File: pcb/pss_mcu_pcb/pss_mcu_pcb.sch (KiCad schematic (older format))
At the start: 50 parts, among them J1 STM32_Prog, J2 UART_Prog, J3 Conn_01x18, J4 Conn_01x18, SW1 Boot, SW2 EN, SW3 SW_Push, U1 LM3940IMP-3.3_NOPB, U2 LM358, U3 STM32F030K6Tx, U4 ESP32-WROOM-32U

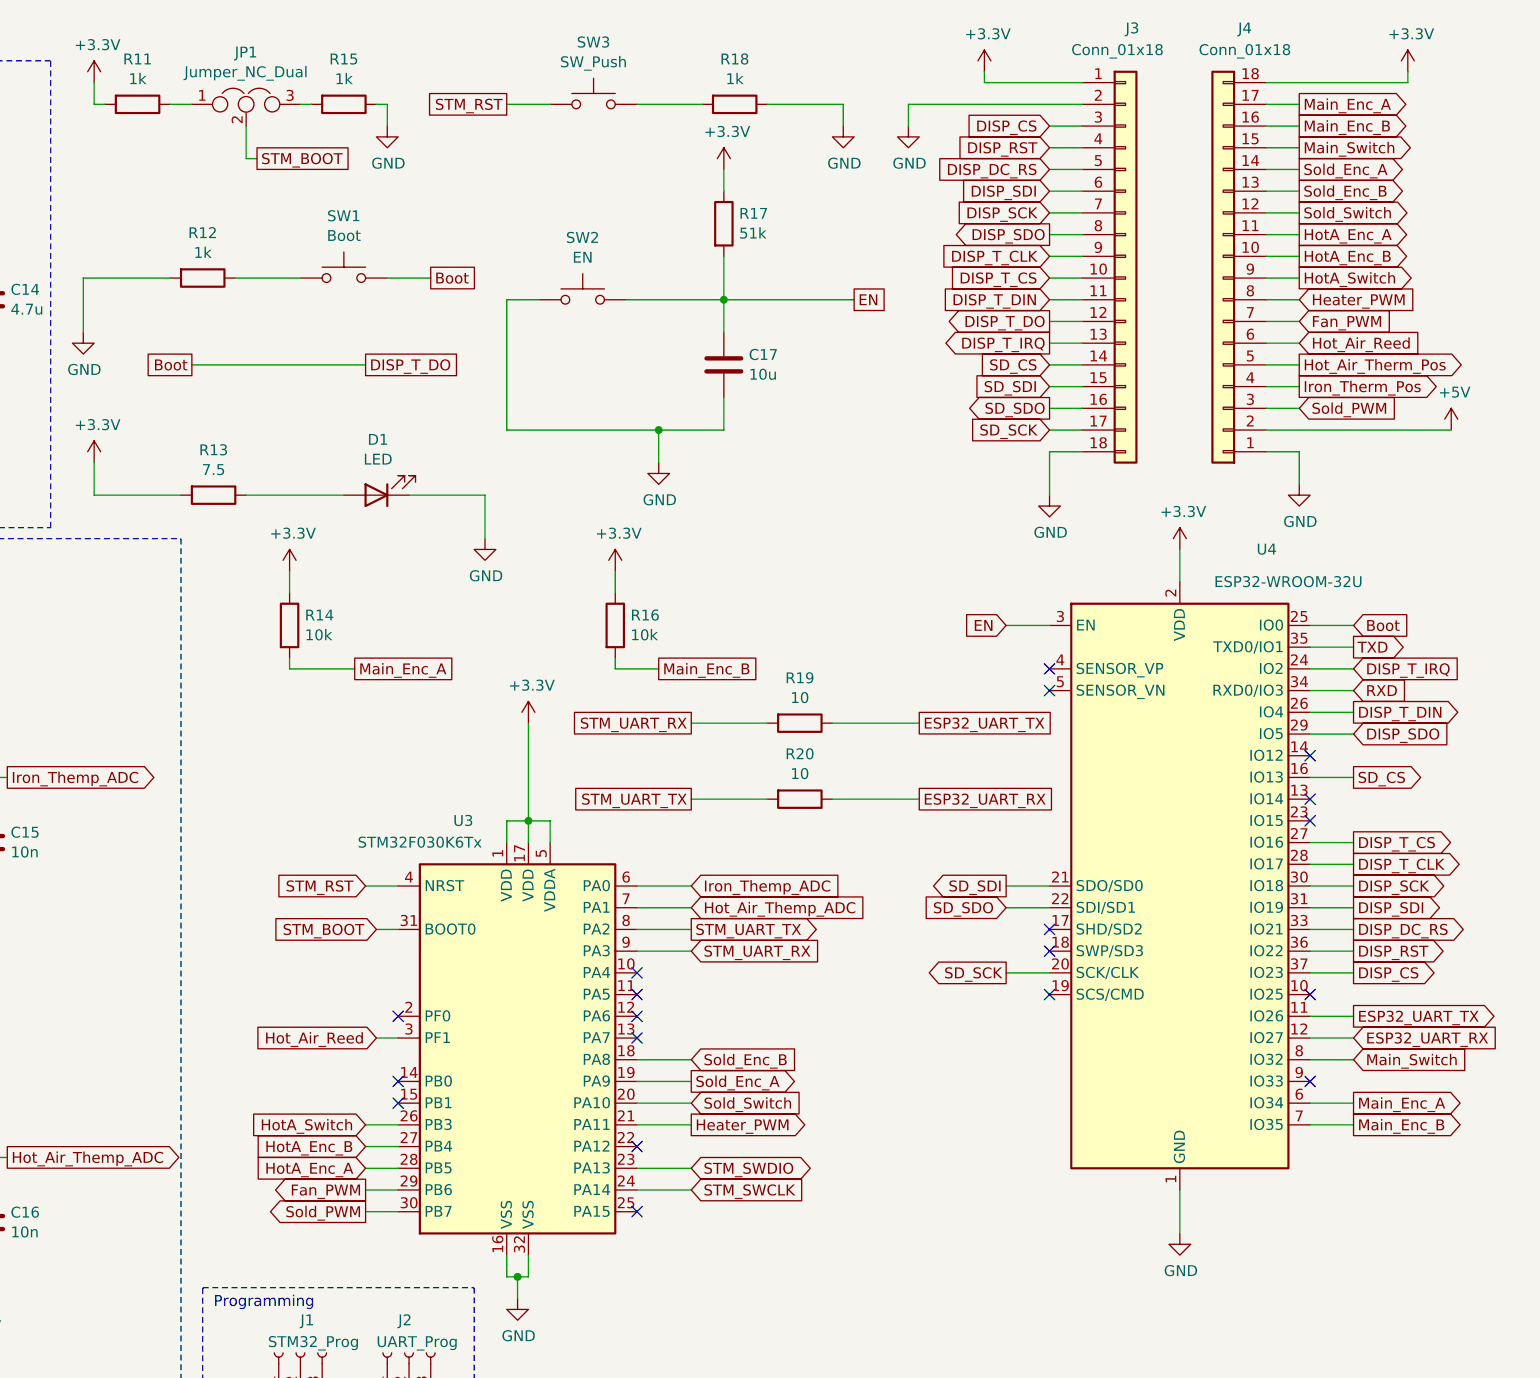
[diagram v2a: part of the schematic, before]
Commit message: Change elements placement
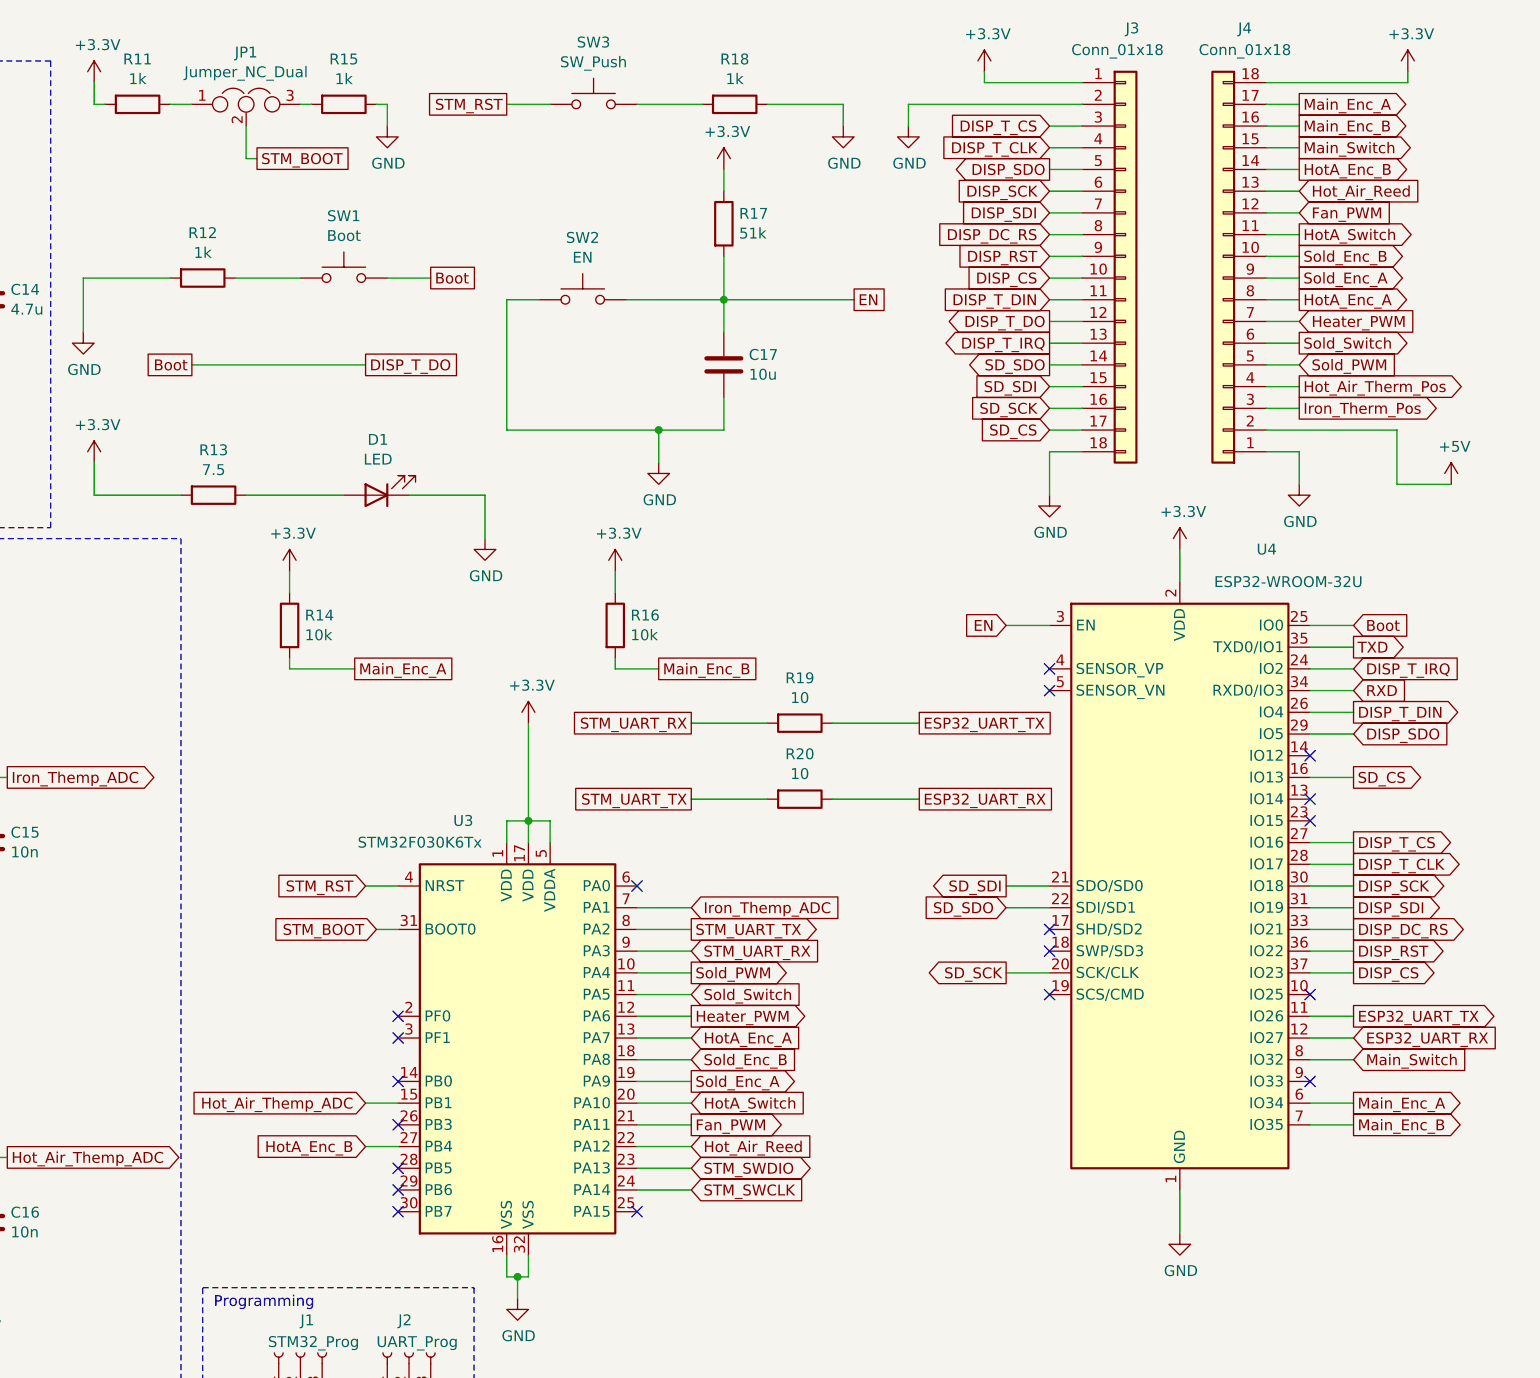
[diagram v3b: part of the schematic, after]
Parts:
- D1: footprint LED_THT:LED_D5.0mm -> LED_SMD:LED_0603_1608Metric_Pad1.05x0.95mm_HandSolder
- SW1, SW2, SW3: footprint Button_Switch_SMD:SW_SPST_B3S-1000 -> Button_Switch_SMD:SW_SPST_B3U-1000P
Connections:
- net DISP_CS: now also J3.10 (Pin_10); no longer J3.3 (Pin_3)
- net DISP_DC_RS: now also J3.8 (Pin_8); no longer J3.5 (Pin_5)
- net DISP_RST: now also J3.9 (Pin_9); no longer J3.4 (Pin_4)
- net DISP_SCK: now also J3.6 (Pin_6); no longer J3.7 (Pin_7)
- net DISP_SDI: now also J3.7 (Pin_7); no longer J3.6 (Pin_6)
- net DISP_SDO: now also J3.5 (Pin_5); no longer J3.8 (Pin_8)
- net DISP_T_CLK: now also J3.4 (Pin_4); no longer J3.9 (Pin_9)
- net DISP_T_CS: now also J3.3 (Pin_3); no longer J3.10 (Pin_10)
- net Fan_PWM: now also J4.12 (Pin_12), U3.21 (PA11); no longer J4.7 (Pin_7), U3.29 (PB6)
- net Heater_PWM: now also J4.7 (Pin_7), U3.12 (PA6); no longer J4.8 (Pin_8), U3.21 (PA11)
- net HotA_Enc_A: now also J4.8 (Pin_8), U3.13 (PA7); no longer J4.11 (Pin_11), U3.28 (PB5)
- net HotA_Enc_B: now also J4.14 (Pin_14); no longer J4.10 (Pin_10)
- net HotA_Switch: now also J4.11 (Pin_11), U3.20 (PA10); no longer J4.9 (Pin_9), U3.26 (PB3)
- net Hot_Air_Reed: now also J4.13 (Pin_13), U3.22 (PA12); no longer J4.6 (Pin_6), U3.3 (PF1)
- net Hot_Air_Themp_ADC: now also U3.15 (PB1); no longer U3.7 (PA1)
- net Hot_Air_Therm_Pos: now also J4.4 (Pin_4); no longer J4.5 (Pin_5)
- net Iron_Themp_ADC: now also U3.7 (PA1); no longer U3.6 (PA0)
- net Iron_Therm_Pos: now also J4.3 (Pin_3); no longer J4.4 (Pin_4)
- net SD_CS: now also J3.17 (Pin_17); no longer J3.14 (Pin_14)
- net SD_SCK: now also J3.16 (Pin_16); no longer J3.17 (Pin_17)
- net SD_SDO: now also J3.14 (Pin_14); no longer J3.16 (Pin_16)
- net Sold_Enc_A: now also J4.9 (Pin_9); no longer J4.14 (Pin_14)
- net Sold_Enc_B: now also J4.10 (Pin_10); no longer J4.13 (Pin_13)
- net Sold_PWM: now also J4.5 (Pin_5), U3.10 (PA4); no longer J4.3 (Pin_3), U3.30 (PB7)
- net Sold_Switch: now also J4.6 (Pin_6), U3.11 (PA5); no longer J4.12 (Pin_12), U3.20 (PA10)
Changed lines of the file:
@@
 F 0 "SW2" H 7100 2085 50  0000 C CNN
 F 1 "EN" H 7100 1994 50  0000 C CNN
-F 2 "Button_Switch_SMD:SW_SPST_B3S-1000" H 7100 2000 50  0001 C CNN
+F 2 "Button_Switch_SMD:SW_SPST_B3U-1000P" H 7100 2000 50  0001 C CNN
 F 3 "~" H 7100 2000 50  0001 C CNN
 	1    7100 1800
@@
 F 0 "SW1" H 6000 1985 50  0000 C CNN
 F 1 "Boot" H 6000 1894 50  0000 C CNN
-F 2 "Button_Switch_SMD:SW_SPST_B3S-1000" H 6000 1900 50  0001 C CNN
+F 2 "Button_Switch_SMD:SW_SPST_B3U-1000P" H 6000 1900 50  0001 C CNN
 F 3 "~" H 6000 1900 50  0001 C CNN
 	1    6000 1700
@@
 F 0 "D1" H 6143 2445 50  0000 C CNN
 F 1 "LED" H 6143 2536 50  0000 C CNN
-F 2 "LED_THT:LED_D5.0mm" H 6150 2700 50  0001 C CNN
+F 2 "LED_SMD:LED_0603_1608Metric_Pad1.05x0.95mm_HandSolder" H 6150 2700 50  0001 C CNN
 F 3 "~" H 6150 2700 50  0001 C CNN
 	1    6150 2700
@@
 F 0 "SW3" H 7150 1185 50  0000 C CNN
 F 1 "SW_Push" H 7150 1094 50  0000 C CNN
-F 2 "Button_Switch_SMD:SW_SPST_B3S-1000" H 7150 1100 50  0001 C CNN
+F 2 "Button_Switch_SMD:SW_SPST_B3U-1000P" H 7150 1100 50  0001 C CNN
 F 3 "~" H 7150 1100 50  0001 C CNN
 	1    7150 900
@@
 $EndComp
 NoConn ~ 6250 5100
-NoConn ~ 7350 5000
-NoConn ~ 7350 5100
-NoConn ~ 7350 5200
-Wire Wire Line
-	6100 5800 6250 5800
 Wire Wire Line
 	6100 5700 6250 5700
 Wire Wire Line
-	6100 5600 6250 5600
-Wire Wire Line
 	7600 5600 7350 5600
-Wire Wire Line
-	6250 5900 6100 5900
-Wire Wire Line
-	6250 5200 6150 5200
-NoConn ~ 7350 5700
-NoConn ~ 6250 5500
-NoConn ~ 6250 5400
-Text GLabel 7600 5600 2    50   Output ~ 0
+Text GLabel 7600 5100 2    50   Output ~ 0
 Heater_PWM
-Wire Wire Line
-	6250 6000 6100 6000
-Text GLabel 6100 6000 0    50   Output ~ 0
+Text GLabel 7600 4900 2    50   Output ~ 0
 Sold_PWM
-Text GLabel 6150 5200 0    50   Input ~ 0
+Text GLabel 7600 5700 2    50   Input ~ 0
 Hot_Air_Reed
 Wire Wire Line
@@
 Text GLabel 7600 5900 2    50   Input ~ 0
 STM_SWCLK
-Text GLabel 6100 5900 0    50   Output ~ 0
+Text GLabel 7600 5600 2    50   Output ~ 0
 Fan_PWM
 Wire Wire Line
 	7350 5500 7600 5500
-Text GLabel 6100 5600 0    50   Input ~ 0
+Text GLabel 7600 5500 2    50   Input ~ 0
 HotA_Switch
 Wire Wire Line
@@
 Wire Wire Line
 	7350 5300 7600 5300
-Text GLabel 6100 5800 0    50   Input ~ 0
+Text GLabel 7600 5200 2    50   Input ~ 0
 HotA_Enc_A
 Text GLabel 7600 5300 2    50   Input ~ 0
@@
 Text GLabel 7600 5400 2    50   Output ~ 0
 Sold_Enc_A
-NoConn ~ 7350 4900
-Text GLabel 7600 5500 2    50   Input ~ 0
+Text GLabel 7600 5000 2    50   Input ~ 0
 Sold_Switch
 Wire Wire Line
@@
 Text GLabel 7600 4700 2    50   Output ~ 0
 STM_UART_TX
-Wire Wire Line
-	7600 4600 7350 4600
-Wire Wire Line
-	7350 4500 7600 4500
+Text GLabel 6100 5500 0    50   Input ~ 0
+Hot_Air_Themp_ADC
 Text GLabel 7600 4600 2    50   Input ~ 0
-Hot_Air_Themp_ADC
-Text GLabel 7600 4500 2    50   Input ~ 0
 Iron_Themp_ADC
 Wire Wire Line
@@
 Wire Wire Line
 	9250 2100 9400 2100
-Text GLabel 10400 2100 2    50   Output ~ 0
-Hot_Air_Therm_Pos
 Wire Wire Line
 	9250 2000 9400 2000
@@
 L power:+5V #PWR038
 U 1 1 5FF764FA
-P 11100 2400
-F 0 "#PWR038" H 11100 2250 50  0001 C CNN
-F 1 "+5V" H 11115 2573 50  0000 C CNN
-F 2 "" H 11100 2400 50  0001 C CNN
-F 3 "" H 11100 2400 50  0001 C CNN
-	1    11100 2400
+P 11100 2650
+F 0 "#PWR038" H 11100 2500 50  0001 C CNN
+F 1 "+5V" H 11115 2823 50  0000 C CNN
+F 2 "" H 11100 2650 50  0001 C CNN
+F 3 "" H 11100 2650 50  0001 C CNN
+	1    11100 2650
 	1    0    0    -1
 $EndComp
@@
 Text GLabel 10400 1000 2    50   Output ~ 0
 Main_Enc_B
-Text GLabel 10400 1300 2    50   Output ~ 0
-Sold_Enc_B
 Text GLabel 10400 1200 2    50   Output ~ 0
-Sold_Enc_A
-Text GLabel 10400 1400 2    50   Output ~ 0
-Sold_Switch
-Text GLabel 10400 1500 2    50   Output ~ 0
-HotA_Enc_A
-Text GLabel 10400 1600 2    50   Output ~ 0
 HotA_Enc_B
-Text GLabel 10400 1700 2    50   Output ~ 0
-HotA_Switch
-Text GLabel 10400 2300 2    50   Input ~ 0
-Sold_PWM
-Text GLabel 10400 1800 2    50   Input ~ 0
-Heater_PWM
 Text GLabel 10400 1100 2    50   Output ~ 0
 Main_Switch
 Text GLabel 10400 900  2    50   Output ~ 0
 Main_Enc_A
-Text GLabel 9250 1200 0    50   Input ~ 0
+Text GLabel 9250 1500 0    50   Input ~ 0
 DISP_DC_RS
+Text GLabel 9250 1700 0    50   Input ~ 0
+DISP_CS
+Text GLabel 9250 1400 0    50   Input ~ 0
+DISP_SDI
+Text GLabel 9250 1300 0    50   Input ~ 0
+DISP_SCK
+Text GLabel 9250 1600 0    50   Input ~ 0
+DISP_RST
+Text GLabel 9250 1100 0    50   Input ~ 0
+DISP_T_CLK
 Text GLabel 9250 1000 0    50   Input ~ 0
-DISP_CS
-Text GLabel 9250 1300 0    50   Input ~ 0
-DISP_SDI
-Text GLabel 9250 1400 0    50   Input ~ 0
-DISP_SCK
-Text GLabel 9250 1100 0    50   Input ~ 0
-DISP_RST
-Text GLabel 9250 1600 0    50   Input ~ 0
-DISP_T_CLK
-Text GLabel 9250 1700 0    50   Input ~ 0
 DISP_T_CS
 Text GLabel 9250 1800 0    50   Input ~ 0
@@
 Text GLabel 9250 2000 0    50   Output ~ 0
 DISP_T_IRQ
-Text GLabel 9250 1500 0    50   Output ~ 0
+Text GLabel 9250 1200 0    50   Output ~ 0
 DISP_SDO
-Text GLabel 9250 2100 0    50   Input ~ 0
+Text GLabel 9250 2400 0    50   Input ~ 0
 SD_CS
 Wire Wire Line
@@
 Wire Wire Line
 	10250 1200 10400 1200
-Wire Wire Line
-	10250 1300 10400 1300
-Wire Wire Line
-	10250 1400 10400 1400
-Wire Wire Line
-	10250 1500 10400 1500
-Wire Wire Line
-	10250 1600 10400 1600
-Wire Wire Line
-	10250 1700 10400 1700
-Wire Wire Line
-	10250 1800 10400 1800
-Wire Wire Line
-	10250 1900 10400 1900
-Text GLabel 9250 2400 0    50   Input ~ 0
+Text GLabel 9250 2300 0    50   Input ~ 0
 SD_SCK
-Text GLabel 9250 2300 0    50   Output ~ 0
+Text GLabel 9250 2100 0    50   Output ~ 0
 SD_SDO
 $Comp
@@
 	-1   0    0    1
 $EndComp
-Text GLabel 10400 2200 2    50   Output ~ 0
-Iron_Therm_Pos
 Wire Wire Line
 	10250 2100 10400 2100
-Text GLabel 10400 1900 2    50   Input ~ 0
+Text GLabel 10400 1400 2    50   Input ~ 0
 Fan_PWM
-Wire Wire Line
-	10250 2400 11100 2400
 Wire Wire Line
 	10250 2200 10400 2200
@@
 Text GLabel 8650 3750 2    50   UnSpc ~ 0
 ESP32_UART_TX
-Text GLabel 10400 2000 2    50   Input ~ 0
+Text GLabel 10400 1300 2    50   Input ~ 0
 Hot_Air_Reed
 $Comp
@@
 Connection ~ 1950 2400
 NoConn ~ 7350 6000
+Wire Wire Line
+	10250 1900 10400 1900
+Text GLabel 10400 2300 2    50   Output ~ 0
+Iron_Therm_Pos
+Wire Wire Line
+	10250 1800 10400 1800
+Wire Wire Line
+	10250 1700 10400 1700
+Wire Wire Line
+	10250 1600 10400 1600
+Wire Wire Line
+	10250 1500 10400 1500
+Wire Wire Line
+	10250 1400 10400 1400
+Wire Wire Line
+	10250 1300 10400 1300
+Text GLabel 10400 1700 2    50   Output ~ 0
+Sold_Enc_A
+Text GLabel 10400 2200 2    50   Output ~ 0
+Hot_Air_Therm_Pos
+NoConn ~ 6250 5200
+Wire Wire Line
+	7350 5700 7600 5700
+Wire Wire Line
+	6100 5500 6250 5500
+Wire Wire Line
+	7600 5200 7350 5200
+NoConn ~ 6250 5800
+NoConn ~ 6250 5900
+NoConn ~ 6250 5600
+Wire Wire Line
+	7350 4900 7600 4900
+Wire Wire Line
+	7350 5100 7600 5100
+Wire Wire Line
+	7350 5000 7600 5000
+NoConn ~ 6250 6000
+NoConn ~ 7350 4500
+Text GLabel 10400 1800 2    50   Output ~ 0
+HotA_Enc_A
+Text GLabel 10400 1600 2    50   Output ~ 0
+Sold_Enc_B
+Text GLabel 10400 1500 2    50   Output ~ 0
+HotA_Switch
+Text GLabel 10400 2100 2    50   Input ~ 0
+Sold_PWM
+Text GLabel 10400 1900 2    50   Input ~ 0
+Heater_PWM
+Text GLabel 10400 2000 2    50   Output ~ 0
+Sold_Switch
+Wire Wire Line
+	10250 2400 10850 2400
+Wire Wire Line
+	10850 2400 10850 2650
+Wire Wire Line
+	10850 2650 11100 2650
+Wire Wire Line
+	7350 4600 7600 4600
+NoConn ~ 6250 5400
 $EndSCHEMATC
